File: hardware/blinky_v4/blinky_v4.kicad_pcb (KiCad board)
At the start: 2 copper layers, 120 x 70 mm, 199 parts, among them J1 RJ45, J2 Conn_01x06_Pin, J3 Conn_01x05_Pin, J4 Conn_01x07, J5 Conn_01x06_Pin, J6 Conn_01x04_Pin, J7 Conn_01x04_Pin, J8 Conn_01x03_Pin, J9 Conn_02x10_Odd_Even, Q1 2N7002, Q2 2N7002, Q3 2N7002, Q4 2N7002, Q5 2N7002, Q6 2N7002, Q7 2N7002, Q8 2N7002, U1 ADA4807-1, U10 STM32F405RGTx, U11 AMS1117-3.3, U12 BA50DD0WHFP-TR, U2 SN74LVC1G14DBV, U3 SN74LVC1G14DBV, U4 ADA4807-1, U5 ADA4807-1, U6 TLV3603DCKR, U7 SN74LVC1G14DBV, U8 TLV3603DCKR, U9 L78L05_SOT89, Y1 AOCJY4A-10.000MHZ-SW, Y2 16MHz

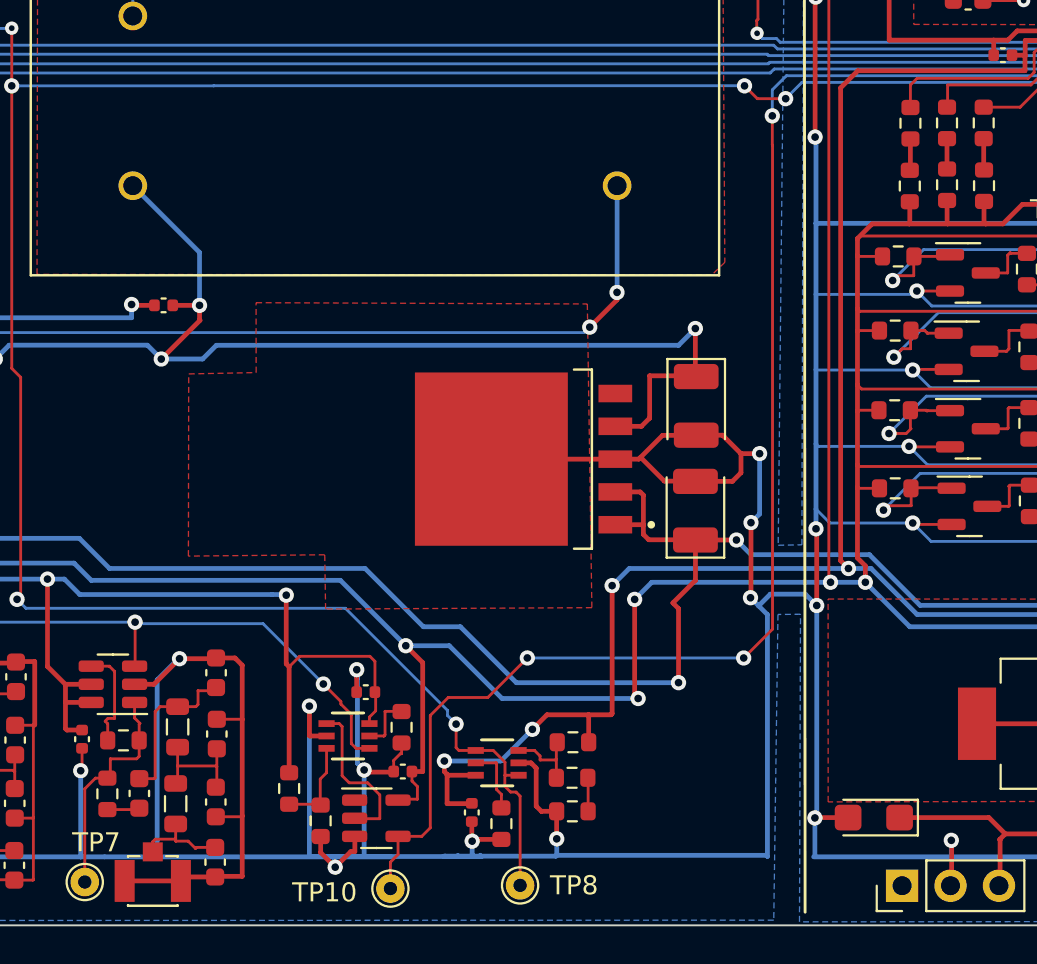
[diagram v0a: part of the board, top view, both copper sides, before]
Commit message: add board 2 board power connector
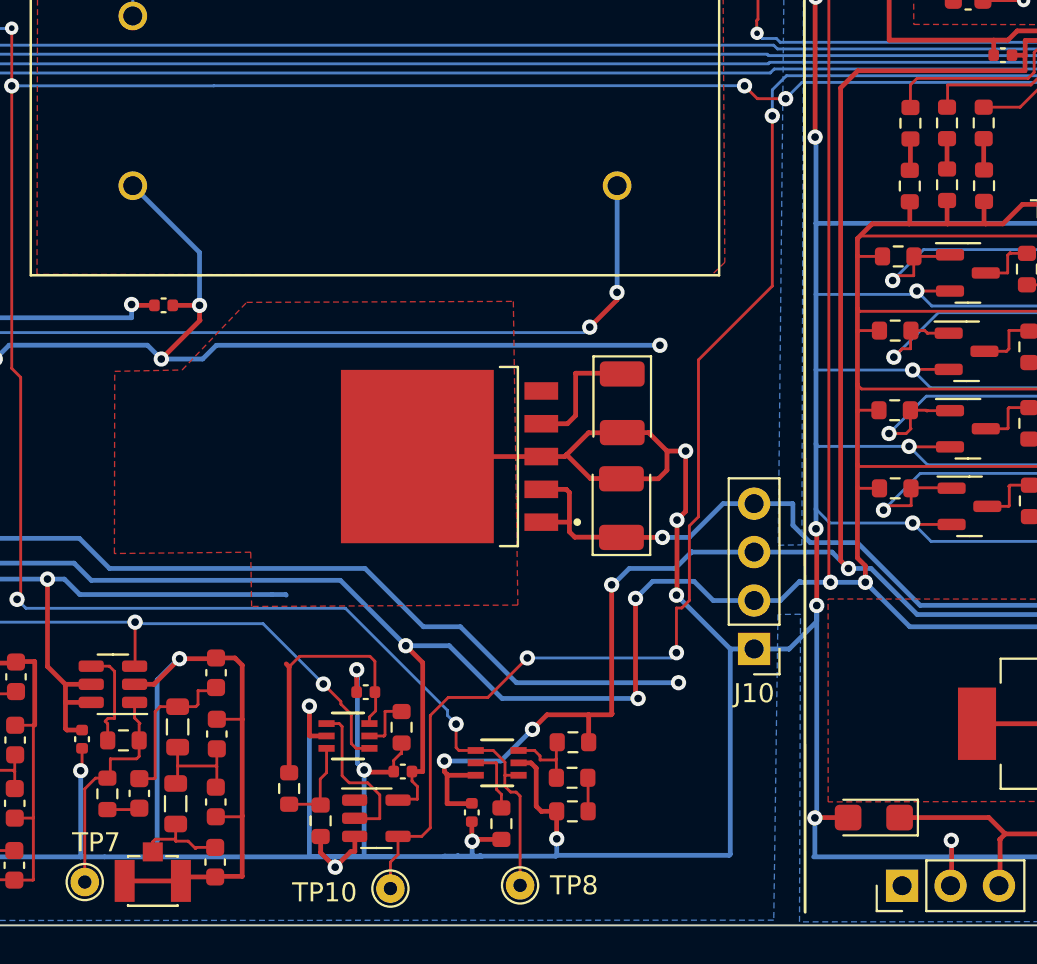
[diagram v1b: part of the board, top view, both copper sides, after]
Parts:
- added J10: Conn_01x04, Connector_PinHeader_2.54mm:PinHeader_1x04_P2.54mm_Vertical, F.Cu at (160.5, 105.5)
- moved C44 3.88 mm to (153.5, 98.1)
- moved C42 3.88 mm to (153.6, 92.6)
- moved U12 3.88 mm to (144.5, 95.4)
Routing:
- net +5V: track 128.5 -> 123.9 mm
- net +5VA: track 114.0 -> 110.4 mm, vias 6 -> 5
- net EXT_CLK_IN: track 89.2 -> 87.1 mm
- net +6V: track 141.1 -> 139.1 mm
- net GND: track 1068.9 -> 1070.3 mm
- net +3.3V: track 455.2 -> 456.4 mm
- net +3.3VA: track 114.1 -> 114.9 mm

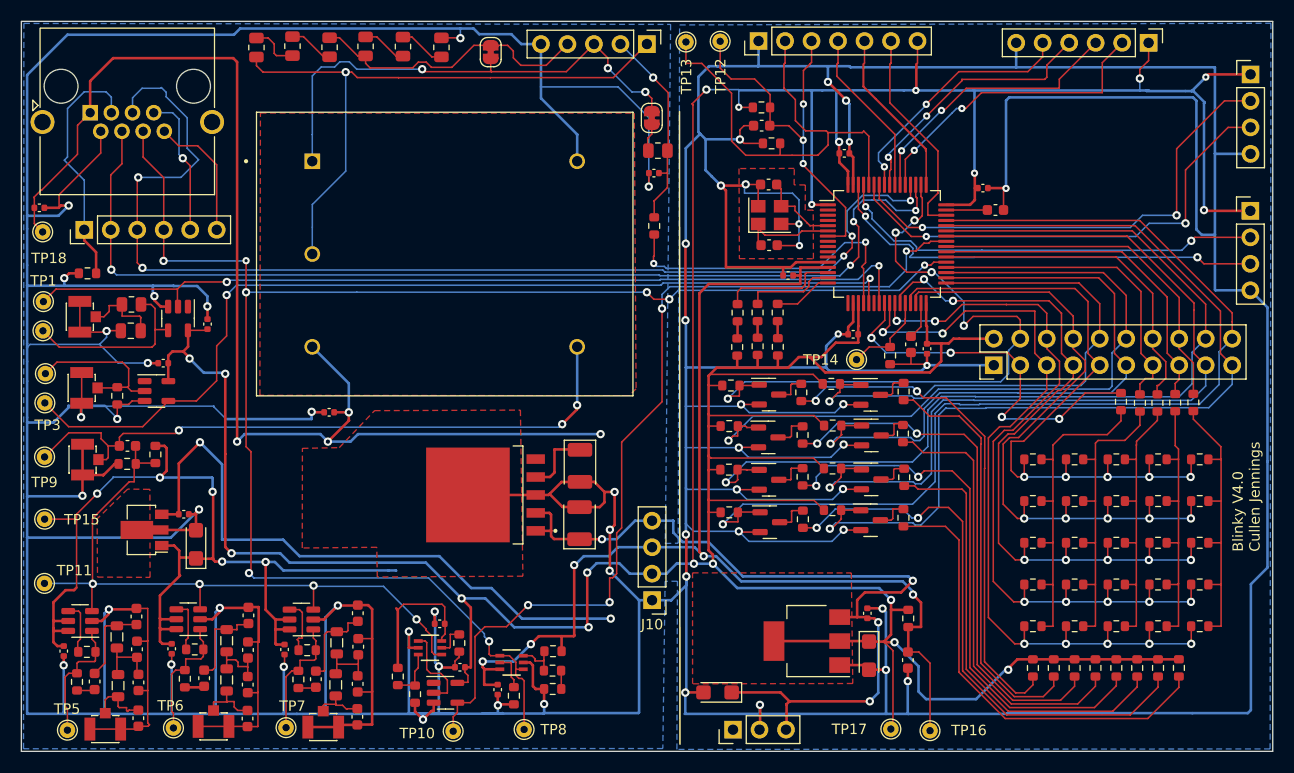
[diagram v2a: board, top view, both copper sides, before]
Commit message: update values for R and G LED
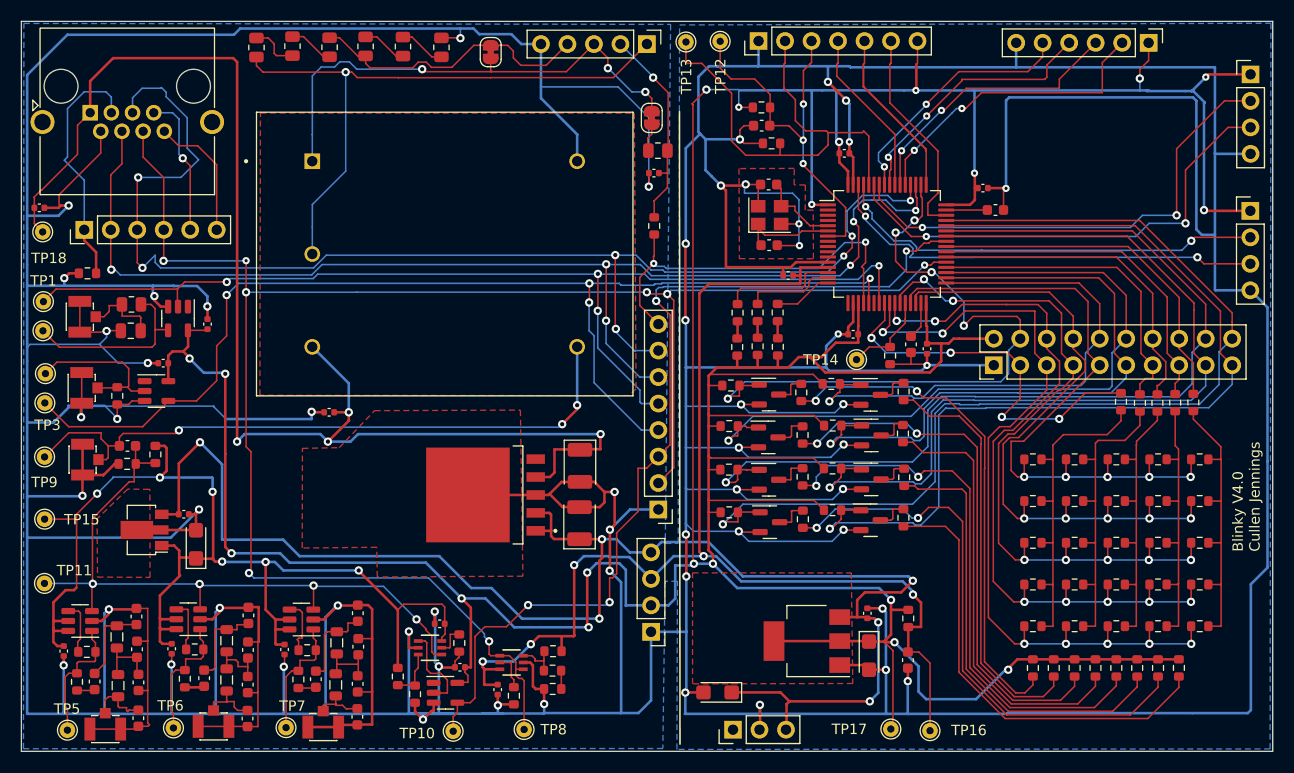
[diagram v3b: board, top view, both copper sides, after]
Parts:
- added J11: Conn_01x08, Connector_PinHeader_2.54mm:PinHeader_1x08_P2.54mm_Vertical, F.Cu at (161.1, 96.8)
- D1, D10, D11, D2, D3, D4, D5, D6, D7, D8, D9: value LED -> LED-RED
- D12, D13, D14, D15, D16, D17, D18, D19, D20, D21, D22, D23, D24, D25, D26, D27, D28, D29, D30, D31, D32, D33, D34, D35, D36: value LED -> LED-G
- moved J10 3.04 mm to (160.4, 108.5)
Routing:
- net GPS_PPS: track 158.0 -> 176.6 mm
- net SYNC_IN: track 92.6 -> 110.6 mm, vias 2 -> 4
- net SYNC_OUT: track 86.8 -> 103.1 mm, vias 2 -> 4
- net /GPS_RX1: track 100.5 -> 115.4 mm, vias 4 -> 6
- net /GPS_TX1: track 109.8 -> 124.5 mm, vias 5 -> 7
- net GND: track 1070.3 -> 1080.7 mm
- net OSC_ADJ: track 30.5 -> 37.6 mm
- net +3.3V: track 456.4 -> 462.8 mm
- net +6V: track 139.1 -> 144.5 mm
- net +5V: track 123.9 -> 127.3 mm
- net EXT_CLK_IN: track 87.1 -> 89.3 mm
- net +5VA: track 110.4 -> 111.9 mm, vias 5 -> 6
- net +3.3VA: track 114.9 -> 116.0 mm

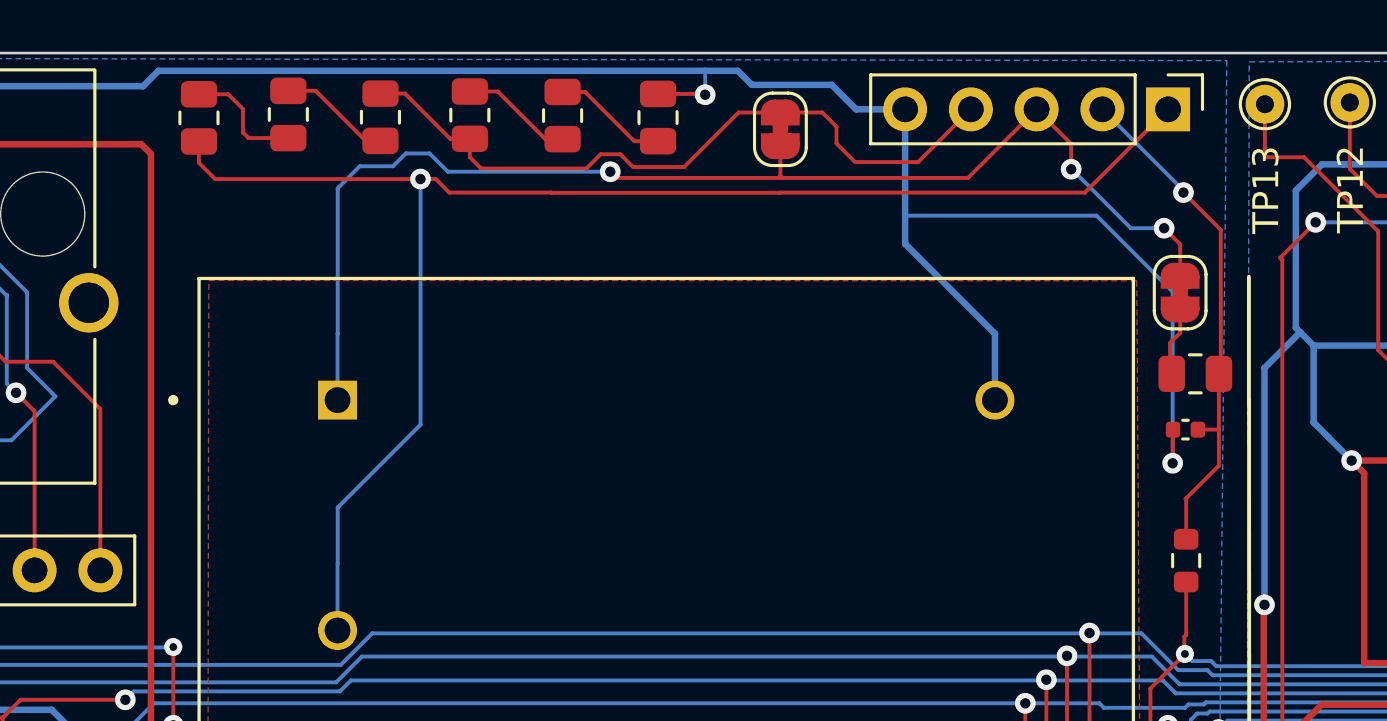
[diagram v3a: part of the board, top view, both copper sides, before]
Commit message: add osc voltage trim adj
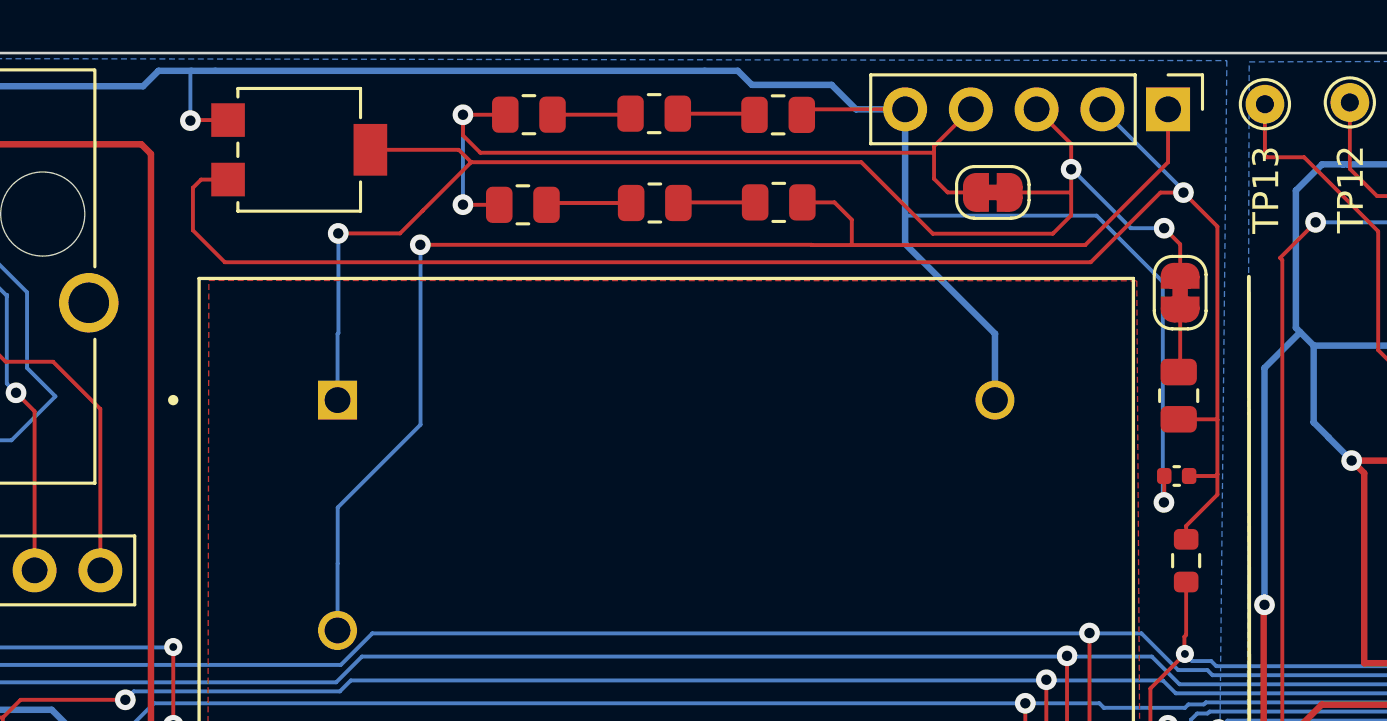
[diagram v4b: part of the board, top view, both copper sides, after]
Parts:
- added RV1: 20K, Potentiometer_SMD:Potentiometer_Bourns_3314G_Vertical, F.Cu at (126.4, 53.7)
- moved R9 22.6 mm to (144.9, 55.8), turned to 180 degrees
- moved R8 14.6 mm to (140.2, 55.8), turned to 180 degrees
- moved JP1 8.56 mm to (153.2, 55.4), turned to 0 degrees
- moved R12 6.46 mm to (135.1, 55.9), turned to 180 degrees
- moved R17 4.64 mm to (144.9, 52.4), turned to 0 degrees
- moved R14 3.54 mm to (140.1, 52.3), turned to 0 degrees
- moved R13 2.28 mm to (135.3, 52.4), turned to 0 degrees
- moved C26 1.82 mm to (160.3, 66.3)
- moved R23 1.06 mm to (160.4, 63.2), turned to 90 degrees
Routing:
- net Net-(J3-Pin_2): track 19.9 -> 64.6 mm
- net Net-(J3-Pin_1): track 58.8 -> 51.7 mm
- net Net-(J3-Pin_3): track 48.0 -> 55.1 mm
- net GND: track 1080.7 -> 1086.6 mm
- net Net-(J3-Pin_4): track 27.8 -> 30.9 mm, vias 0 -> 2
- net Net-(R8-Pad1): track 4.69 -> 2.98 mm
- net Net-(R14-Pad2): track 4.48 -> 2.99 mm
- net Net-(R13-Pad2): track 4.35 -> 3.03 mm
- net Net-(R12-Pad1): track 4.36 -> 3.30 mm

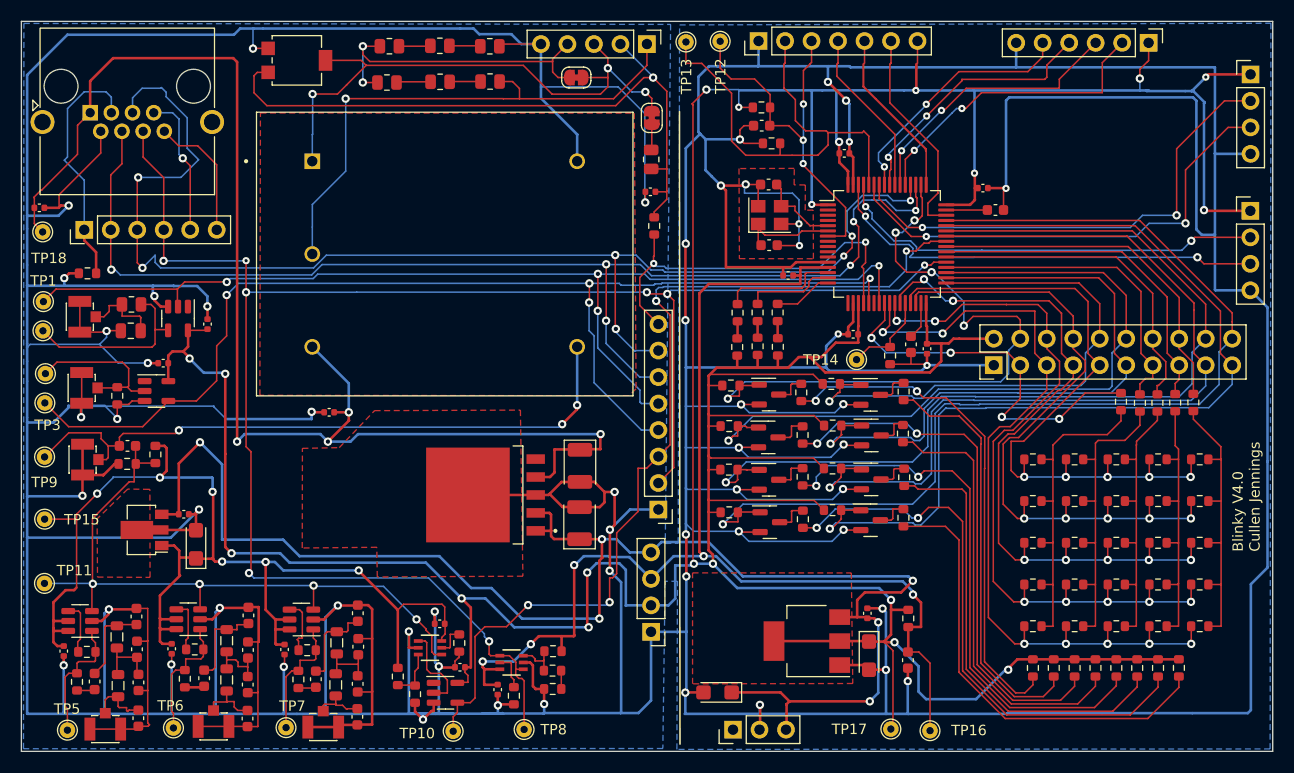
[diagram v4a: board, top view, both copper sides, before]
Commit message: add mount holes
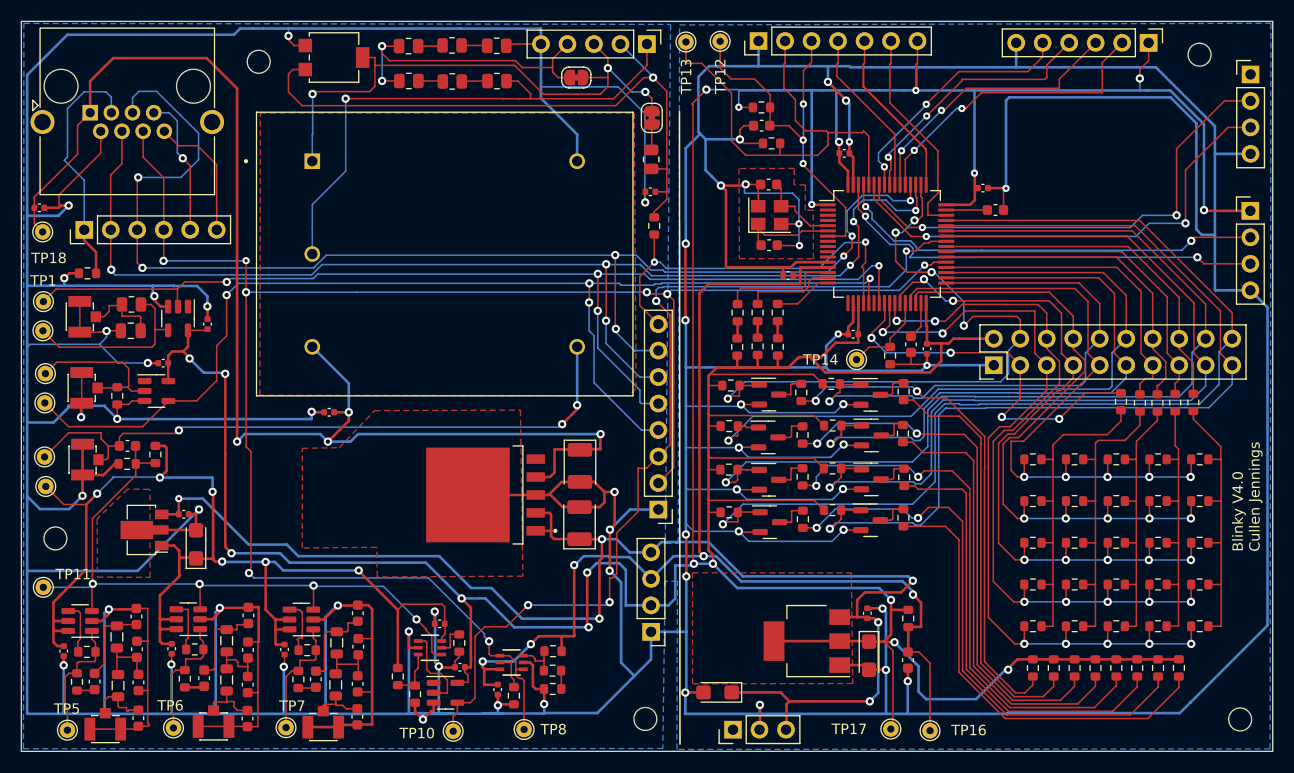
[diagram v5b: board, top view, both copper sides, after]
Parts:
- added H1: M2, MountingHole:MountingHole_2.2mm_M2, F.Cu at (122.8, 53.9)
- added H2: M2, MountingHole:MountingHole_2.2mm_M2, F.Cu at (213.0, 53.2)
- added H3: M2, MountingHole:MountingHole_2.2mm_M2, F.Cu at (159.8, 116.9)
- added H4: M2, MountingHole:MountingHole_2.2mm_M2, F.Cu at (216.9, 116.9)
- added H5: M2, MountingHole:MountingHole_2.2mm_M2, F.Cu at (103.3, 99.6)
- moved RV1 3.58 mm to (130.0, 53.5)
- moved TP15 3.14 mm to (102.3, 94.6)
- moved R12 2.10 mm to (137.2, 55.7)
- moved R13 1.84 mm to (137.1, 52.4)
- moved R14 1.17 mm to (141.3, 52.3)
- moved R8 1.17 mm to (141.3, 55.8)
- moved R17 0.67 mm to (145.6, 52.3)
- moved R9 0.67 mm to (145.6, 55.7)
- moved TP11 0.39 mm to (102.1, 104.3)
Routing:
- net GND: track 1086.6 -> 1073.6 mm
- net +6V: track 144.5 -> 133.8 mm
- net +3.3V: track 462.8 -> 454.9 mm, vias 20 -> 19
- net Net-(J3-Pin_2): track 64.6 -> 61.7 mm
- net /GPS_TX1: track 124.5 -> 122.3 mm
- net Net-(J3-Pin_4): track 30.9 -> 29.4 mm
- net +5V: track 127.3 -> 125.8 mm
- net +5VA: track 111.9 -> 112.9 mm
- net Net-(J3-Pin_3): track 55.1 -> 54.1 mm
- net Net-(R12-Pad1): track 3.30 -> 2.36 mm
- net Net-(R13-Pad2): track 3.03 -> 2.36 mm
